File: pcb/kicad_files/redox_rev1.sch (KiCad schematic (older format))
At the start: 76 parts, among them K0 KEYSW, K1 KEYSW, K10 KEYSW, K11 KEYSW, K12 KEYSW, K13 KEYSW, K14 KEYSW, K15 KEYSW, K16 KEYSW, K2 KEYSW, K20 KEYSW, K21 KEYSW, K22 KEYSW, K23 KEYSW, K24 KEYSW, K25 KEYSW, K26 KEYSW, K3 KEYSW, K30 KEYSW, K31 KEYSW, K32 KEYSW, K33 KEYSW, K34 KEYSW, K35 KEYSW, K36 KEYSW, K4 KEYSW, K40 KEYSW, K41 KEYSW, K42 KEYSW, K43 KEYSW, K44 KEYSW, K45 KEYSW, K46 KEYSW, K5 KEYSW, K6 KEYSW, U1 ProMicro

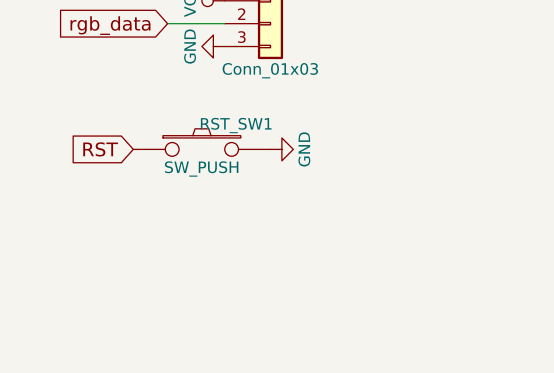
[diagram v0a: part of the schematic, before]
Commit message: Added oled
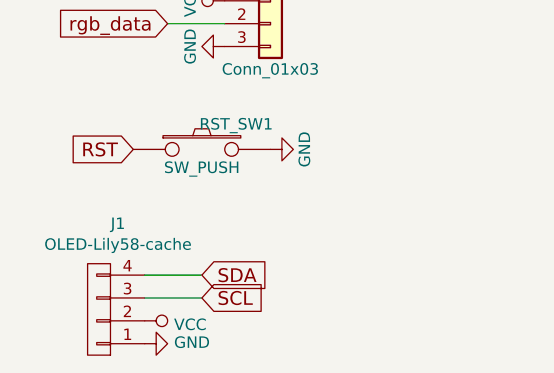
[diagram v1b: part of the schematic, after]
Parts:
- added J1: OLED-Lily58-cache, Lily58_Pro-footprint:OLED_4Pin, symbol Lily58_Pro-rescue:OLED-Lily58-cache
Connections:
- net GND: now also J1.1 (P1)
- net SCL: now also J1.3 (P3)
- net SDA: now also J1.4 (P4)
- net VCC: now also J1.2 (P2)
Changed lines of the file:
@@
 Wire Wire Line
 	1700 3600 1900 3600
+$Comp
+L Lily58_Pro-rescue:OLED-Lily58-cache J1
+U 1 1 600441B6
+P 1000 5450
+F 0 "J1" H 917 5075 50  0000 C CNN
+F 1 "OLED-Lily58-cache" H 917 5166 50  0000 C CNN
+F 2 "Lily58_Pro-footprint:OLED_4Pin" H 1000 5450 50  0001 C CNN
+F 3 "" H 1000 5450 50  0000 C CNN
+	1    1000 5450
+	-1   0    0    1
+$EndComp
+$Comp
+L power:GND #PWR0101
+U 1 1 60058856
+P 1200 5600
+F 0 "#PWR0101" H 1200 5350 50  0001 C CNN
+F 1 "GND" V 1205 5472 50  0000 R CNN
+F 2 "" H 1200 5600 50  0001 C CNN
+F 3 "" H 1200 5600 50  0001 C CNN
+	1    1200 5600
+	0    -1   -1   0
+$EndComp
+$Comp
+L power:VCC #PWR0102
+U 1 1 6005A912
+P 1200 5500
+F 0 "#PWR0102" H 1200 5350 50  0001 C CNN
+F 1 "VCC" V 1217 5628 50  0000 L CNN
+F 2 "" H 1200 5500 50  0001 C CNN
+F 3 "" H 1200 5500 50  0001 C CNN
+	1    1200 5500
+	0    1    1    0
+$EndComp
+Text GLabel 1450 5400 2    60   Input ~ 0
+SCL
+Text GLabel 1450 5300 2    60   Input ~ 0
+SDA
+Wire Wire Line
+	1200 5400 1450 5400
+Wire Wire Line
+	1200 5300 1450 5300
 $EndSCHEMATC

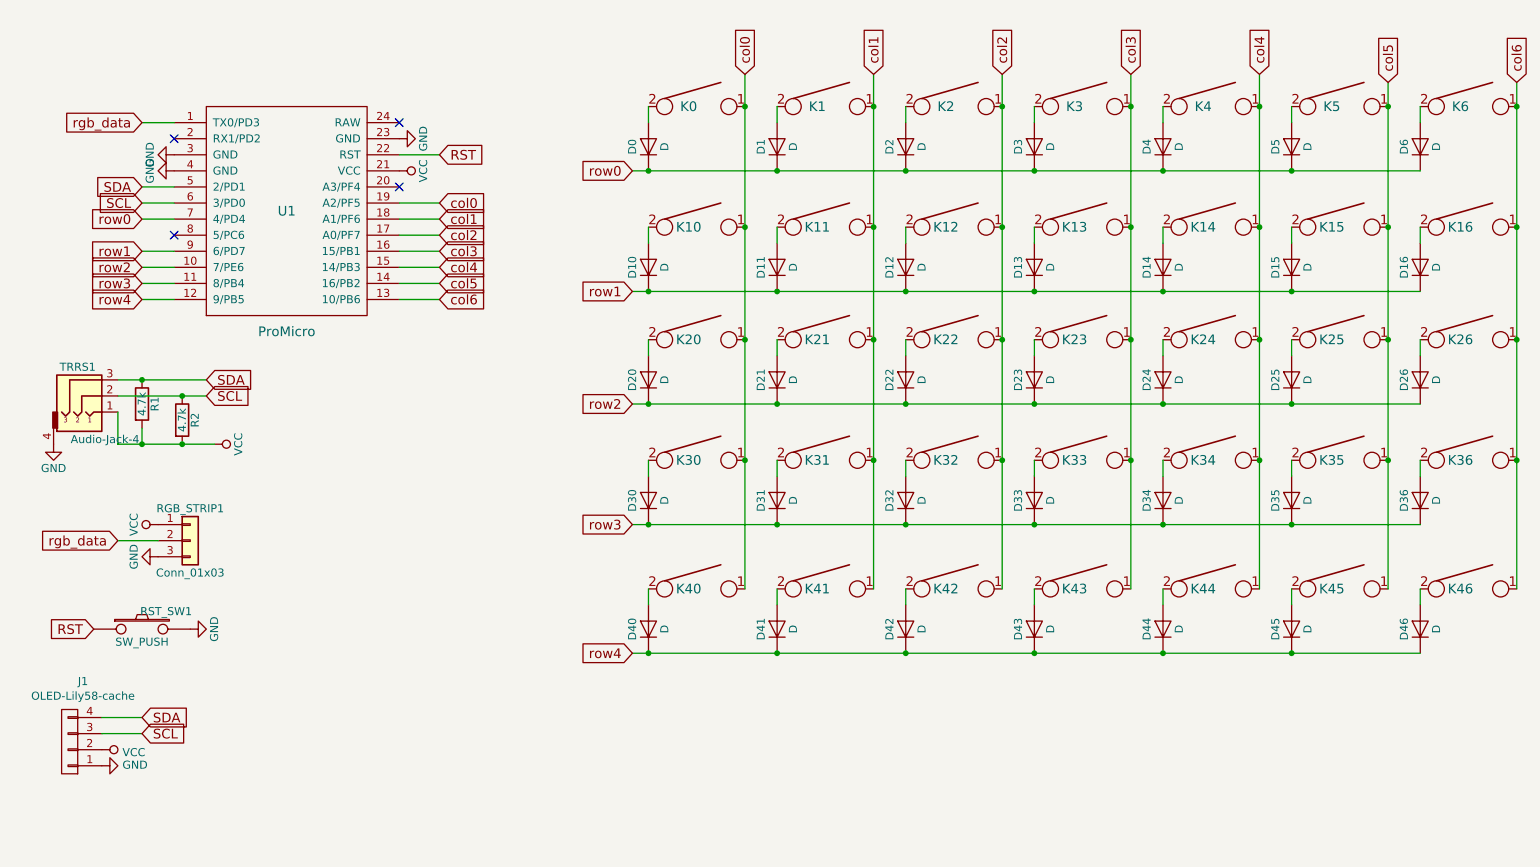
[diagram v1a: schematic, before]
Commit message: Completed pcb routing
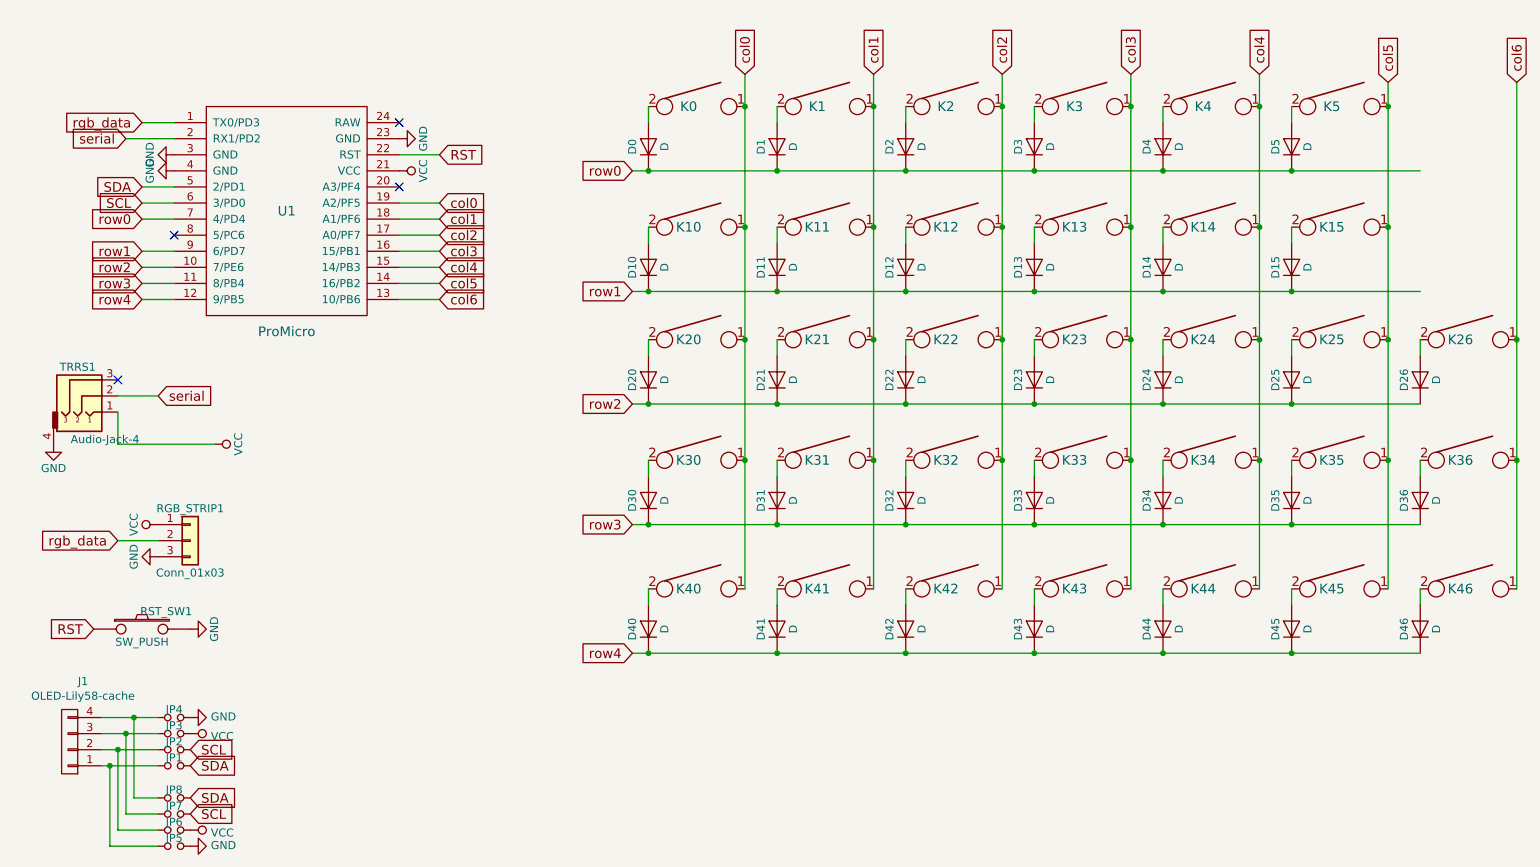
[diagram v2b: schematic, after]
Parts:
- removed D16, D6: D, Keebio-Parts:Diode-dual, symbol Device:D
- removed K16, K6: KEYSW, keyswitches:SW_MX_reversible, symbol redox_rev1-rescue:KEYSW
- removed R1, R2: 4.7k, Keebio-Parts:Resistor-Compact, symbol Device:R
- added JP1, JP2, JP3, JP4, JP5, JP6, JP7, JP8: Jumper_NO_Small, Lily58_Pro-footprint:Jumper, symbol Device:Jumper_NO_Small
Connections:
- net GND: now also JP4.2, JP5.2; no longer J1.1 (P1)
- net SCL: now also JP2.2, JP7.2; no longer J1.3 (P3), TRRS1.2
- net SDA: now also JP1.2, JP8.2; no longer J1.4 (P4), TRRS1.3
- net VCC: now also JP3.2, JP6.2; no longer J1.2 (P2)
- net serial: now reaches U1.2 (RX1/PD2)
- net serial: now also TRRS1.2
- new net: J1.1 (P1), JP1.1, JP5.1
- new net: J1.2 (P2), JP2.1, JP6.1
- new net: J1.3 (P3), JP3.1, JP7.1
- new net: J1.4 (P4), JP4.1, JP8.1
